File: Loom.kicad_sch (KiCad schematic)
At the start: 49 parts

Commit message: Minor changes
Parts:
- LMB: symbol Connector_Generic:Conn_01x03 -> Connector_Generic:Conn_01x04
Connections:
- net SENGND: now also LMB.4 (Pin_4); no longer LMB.3 (Pin_3)
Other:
- note added: "Pwr (12V) Sig1 Sig2 Gnd (SENGND)"
- note removed: "Pwr (12V) Sig Gnd (SENGND)"
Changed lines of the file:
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@@
 	(rectangle
 		(start 297.18 15.24)
-		(end 340.36 160.02)
+		(end 340.36 162.56)
 		(stroke
 			(width 0)
@@
 		)
 	)
-	(text "Pwr (12V)\nSig\nGnd (SENGND)"
+	(text "Pwr (12V)\nSig1\nSig2\nGnd (SENGND)\n "
 		(exclude_from_sim no)
-		(at 317.5 149.86 0)
+		(at 317.5 152.4 0)
 		(effects
 			(font
@@
 	(text "Engine Sensors"
 		(exclude_from_sim no)
-		(at 297.18 160.02 0)
+		(at 297.18 162.56 0)
 		(effects
 			(font
@@
 	)
 	(junction
+		(at 294.64 154.94)
+		(diameter 0)
+		(color 0 0 0 0)
+	)
+	(junction
 		(at 294.64 99.06)
 		(diameter 0)
@@
 	)
 	(junction
+		(at 485.14 259.08)
+		(diameter 0)
+		(color 0 0 0 0)
+	)
+	(junction
 		(at 558.8 160.02)
 		(diameter 0)
@@
 	)
 	(junction
-		(at 474.98 259.08)
+		(at 485.14 317.5)
 		(diameter 0)
 		(color 0 0 0 0)
@@
 	)
 	(junction
+		(at 477.52 208.28)
+		(diameter 0)
+		(color 0 0 0 0)
+	)
+	(junction
 		(at 558.8 170.18)
 		(diameter 0)
@@
 	)
 	(junction
+		(at 477.52 205.74)
+		(diameter 0)
+		(color 0 0 0 0)
+	)
+	(junction
 		(at 401.32 40.64)
 		(diameter 0)
@@
 	)
 	(junction
-		(at 474.98 317.5)
-		(diameter 0)
-		(color 0 0 0 0)
-	)
-	(junction
 		(at 294.64 81.28)
 		(diameter 0)
@@
 	)
 	(junction
-		(at 477.52 187.96)
-		(diameter 0)
-		(color 0 0 0 0)
-	)
-	(junction
 		(at 490.22 40.64)
 		(diameter 0)
@@
 	)
 	(junction
-		(at 294.64 152.4)
-		(diameter 0)
-		(color 0 0 64 1)
-	)
-	(junction
 		(at 558.8 165.1)
 		(diameter 0)
@@
 	)
 	(junction
-		(at 469.9 208.28)
-		(diameter 0)
-		(color 0 0 0 0)
-	)
-	(junction
 		(at 558.8 167.64)
 		(diameter 0)
@@
 	(wire
 		(pts
+			(xy 485.14 317.5) (xy 541.02 317.5)
+		)
+		(stroke
+			(width 0)
+			(type default)
+			(color 255 0 0 1)
+		)
+	)
+	(wire
+		(pts
 			(xy 525.78 111.76) (xy 546.1 111.76)
 		)
@@
 	(wire
 		(pts
-			(xy 469.9 208.28) (xy 469.9 243.84)
+			(xy 477.52 208.28) (xy 477.52 243.84)
 		)
 		(stroke
@@
 	(wire
 		(pts
-			(xy 487.68 259.08) (xy 474.98 259.08)
+			(xy 294.64 154.94) (xy 294.64 233.68)
+		)
+		(stroke
+			(width 0)
+			(type default)
+			(color 0 0 64 1)
+		)
+	)
+	(wire
+		(pts
+			(xy 487.68 259.08) (xy 485.14 259.08)
 		)
 		(stroke
@@
 	(wire
 		(pts
-			(xy 414.02 396.24) (xy 414.02 182.88)
+			(xy 414.02 396.24) (xy 414.02 205.74)
 		)
 		(stroke
@@
 	(wire
 		(pts
-			(xy 210.82 208.28) (xy 469.9 208.28)
+			(xy 210.82 208.28) (xy 477.52 208.28)
 		)
 		(stroke
@@
 	(wire
 		(pts
-			(xy 243.84 228.6) (xy 436.88 228.6)
+			(xy 243.84 228.6) (xy 474.98 228.6)
 		)
 		(stroke
@@
 	(wire
 		(pts
-			(xy 373.38 317.5) (xy 474.98 317.5)
+			(xy 373.38 317.5) (xy 485.14 317.5)
 		)
 		(stroke
@@
 	(wire
 		(pts
-			(xy 436.88 261.62) (xy 487.68 261.62)
+			(xy 474.98 261.62) (xy 487.68 261.62)
 		)
 		(stroke
@@
 	(wire
 		(pts
-			(xy 474.98 259.08) (xy 474.98 241.3)
+			(xy 485.14 259.08) (xy 485.14 241.3)
 		)
 		(stroke
@@
 	(wire
 		(pts
-			(xy 487.68 208.28) (xy 469.9 208.28)
+			(xy 487.68 208.28) (xy 477.52 208.28)
 		)
 		(stroke
@@
 	(wire
 		(pts
-			(xy 474.98 317.5) (xy 541.02 317.5)
-		)
-		(stroke
-			(width 0)
-			(type default)
-			(color 255 0 0 1)
-		)
-	)
-	(wire
-		(pts
 			(xy 203.2 25.4) (xy 132.08 25.4)
 		)
@@
 	(wire
 		(pts
-			(xy 414.02 182.88) (xy 477.52 182.88)
+			(xy 414.02 205.74) (xy 477.52 205.74)
 		)
 		(stroke
@@
 	(wire
 		(pts
-			(xy 294.64 152.4) (xy 294.64 233.68)
-		)
-		(stroke
-			(width 0)
-			(type default)
-			(color 0 0 64 1)
-		)
-	)
-	(wire
-		(pts
 			(xy 152.4 261.62) (xy 38.1 261.62)
 		)
@@
 	(wire
 		(pts
-			(xy 436.88 228.6) (xy 436.88 261.62)
+			(xy 474.98 228.6) (xy 474.98 261.62)
 		)
 		(stroke
@@
 	(wire
 		(pts
-			(xy 294.64 124.46) (xy 294.64 152.4)
+			(xy 294.64 124.46) (xy 294.64 154.94)
 		)
 		(stroke
@@
 	(wire
 		(pts
-			(xy 477.52 182.88) (xy 477.52 187.96)
-		)
-		(stroke
-			(width 0)
-			(type default)
-		)
-	)
-	(wire
-		(pts
 			(xy 373.38 386.08) (xy 373.38 393.7)
 		)
@@
 	(wire
 		(pts
-			(xy 487.68 243.84) (xy 469.9 243.84)
+			(xy 487.68 243.84) (xy 477.52 243.84)
 		)
 		(stroke
@@
 	(wire
 		(pts
-			(xy 487.68 241.3) (xy 474.98 241.3)
+			(xy 487.68 241.3) (xy 485.14 241.3)
 		)
 		(stroke
@@
 	(wire
 		(pts
-			(xy 294.64 152.4) (xy 309.88 152.4)
+			(xy 294.64 154.94) (xy 309.88 154.94)
 		)
 		(stroke
@@
 	(wire
 		(pts
-			(xy 474.98 259.08) (xy 474.98 317.5)
+			(xy 485.14 259.08) (xy 485.14 317.5)
 		)
 		(stroke
@@
 	)
 	(label "SENGND"
-		(at 299.72 152.4 0)
+		(at 299.72 154.94 0)
 		(effects
 			(font
@@
 	)
 	(label "FanSig"
-		(at 459.74 261.62 0)
+		(at 459.74 228.6 0)
 		(effects
 			(font
@@
 	)
 	(label "Shutdown"
-		(at 459.74 182.88 0)
+		(at 459.74 205.74 0)
 		(effects
 			(font
@@
 	)
 	(symbol
-		(lib_id "Connector_Generic:Conn_01x03")
+		(lib_id "Connector_Generic:Conn_01x04")
 		(at 314.96 149.86 0)
 		(unit 1)
@@
 			)
 		)
-		(property "Description" "Generic connector, single row, 01x03, script generated (kicad-library-utils/schlib/autogen/connector/)"
+		(property "Description" "Generic connector, single row, 01x04, script generated (kicad-library-utils/schlib/autogen/connector/)"
 			(at 314.96 149.86 0)
 			(effects
@@
 		(pin "2"
 		)
+		(pin "4"
+		)
 		(instances

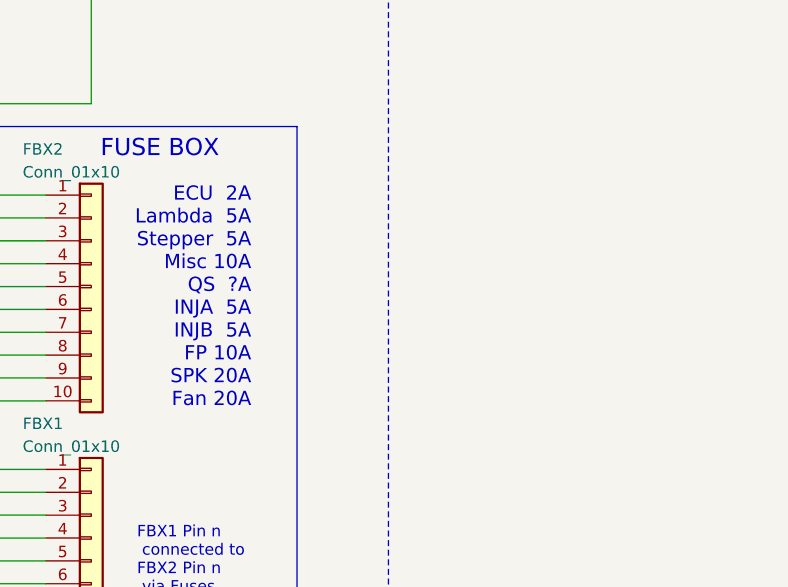
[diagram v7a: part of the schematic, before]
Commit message: Start updating fuses
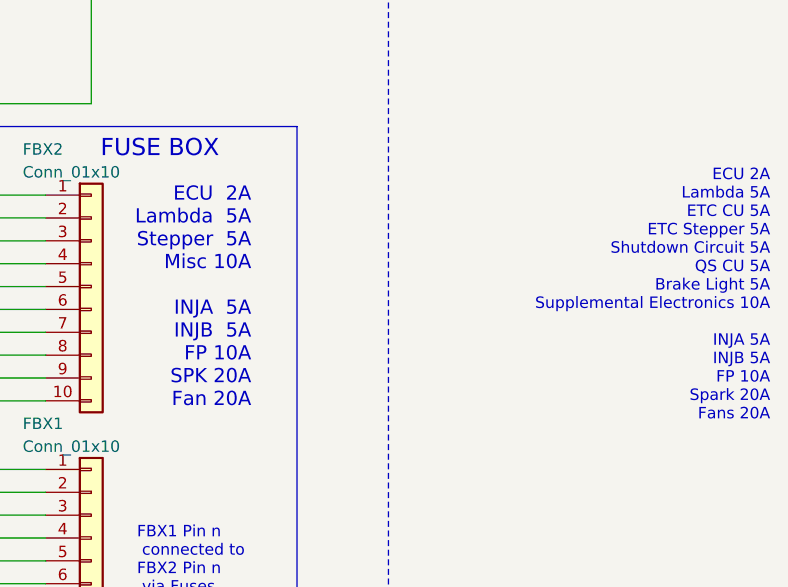
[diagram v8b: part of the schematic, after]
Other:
- note added: "ECU 2A Lambda 5A ETC CU 5A ETC Stepper 5A Shutdown Circuit 5A QS CU 5A Brake Light 5A Supplemental Electronics 10A INJA 5A INJB 5A FP 10A Spark 20A Fans 20A"
- note added: "ECU 2A Lambda 5A Stepper 5A Misc 10A INJA 5A INJB 5A FP 10A SPK 20A Fan 20A"
- note removed: "ECU 2A Lambda 5A Stepper 5A Misc 10A QS ?A INJA 5A INJB 5A FP 10A SPK 20A Fan 20A"
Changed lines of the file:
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@@
 		)
 	)
-	(text "ECU  2A\nLambda  5A\nStepper  5A\nMisc 10A\nQS  ?A\nINJA  5A\nINJB  5A\nFP 10A\nSPK 20A\nFan 20A\n "
+	(text "ECU  2A\nLambda  5A\nStepper  5A\nMisc 10A\n\nINJA  5A\nINJB  5A\nFP 10A\nSPK 20A\nFan 20A\n "
 		(exclude_from_sim no)
 		(at 563.88 292.1 0)
@@
 			)
 			(justify right)
+		)
+	)
+	(text "ECU 2A\nLambda 5A\nETC CU 5A\nETC Stepper 5A\nShutdown Circuit 5A\nQS CU 5A\nBrake Light 5A\nSupplemental Electronics 10A\n\nINJA 5A\nINJB 5A\nFP 10A\nSpark 20A\nFans 20A"
+		(exclude_from_sim no)
+		(at 621.538 290.576 0)
+		(effects
+			(font
+				(size 1.27 1.27)
+			)
+			(justify right)
